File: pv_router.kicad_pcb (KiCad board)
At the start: 4 copper layers, 70 x 70 mm, 83 parts, among them IC1 AP63203WU-7, IC2 ATM90E26-YU-B, J1 Barrel_Jack_Switch_Pin3Ring, J10 Conn_01x03_Pin, J2 AudioJack3, J3 AudioJack3, J4 Barrel_Jack_Switch_Pin3Ring, J5 UART, J6 ToSSR, J7 USB_A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

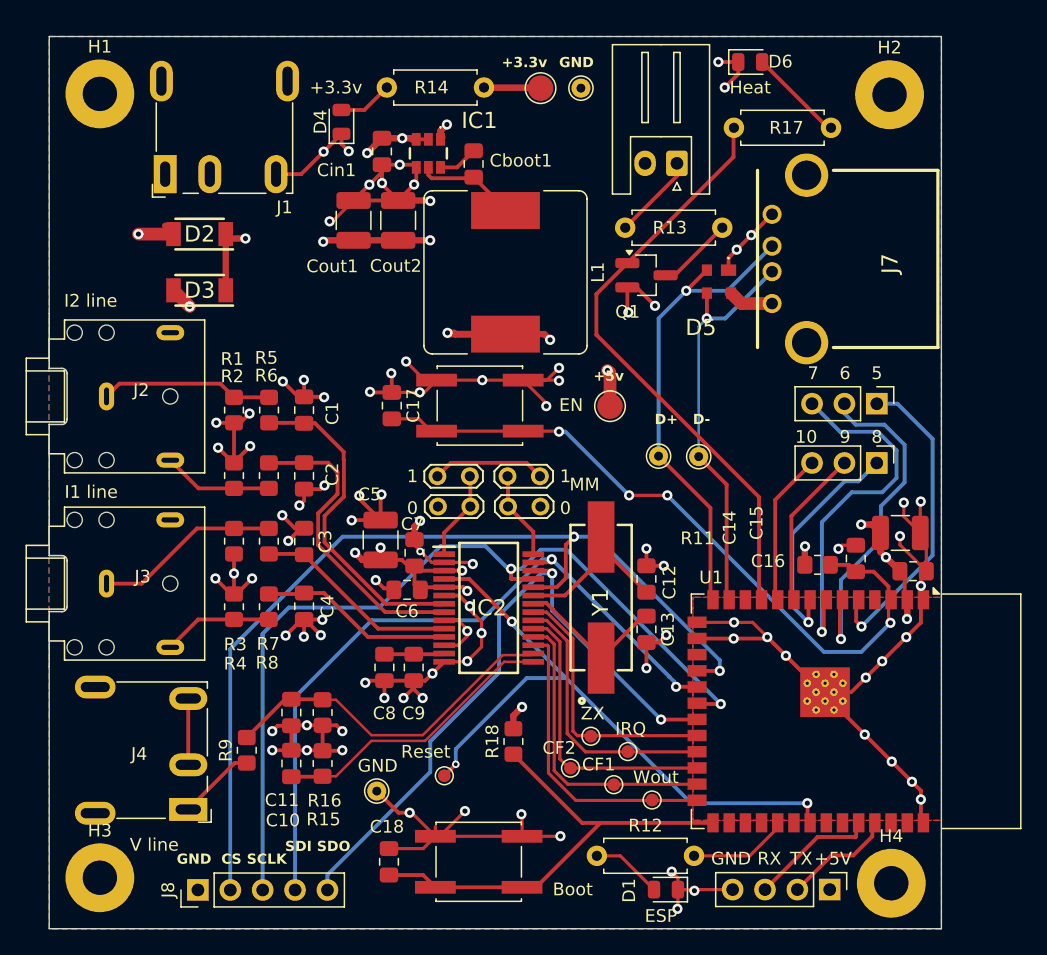
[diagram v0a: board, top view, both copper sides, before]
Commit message: fix: set SMT LED to 1206 size
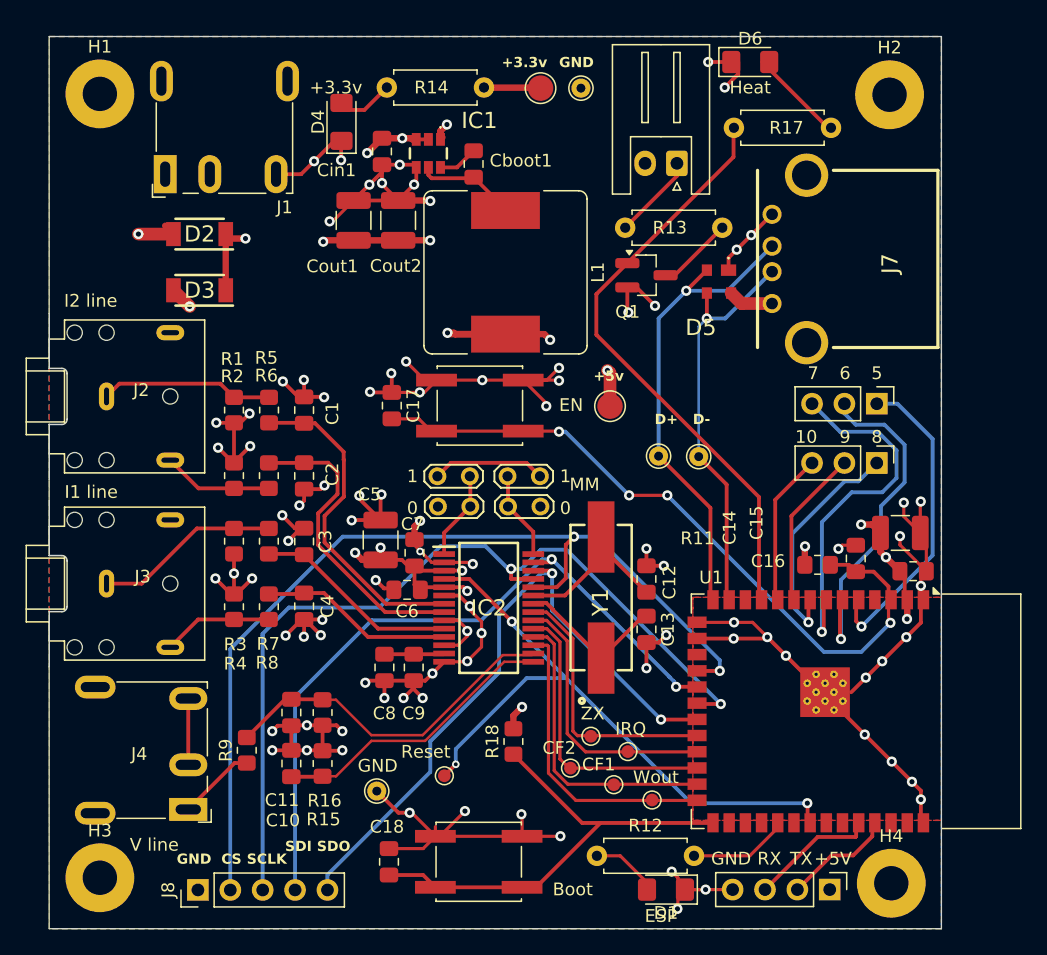
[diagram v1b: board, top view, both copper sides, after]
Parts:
- D1, D4, D6: footprint LED_SMD:LED_0805_2012Metric -> LED_SMD:LED_1206_3216Metric_Pad1.42x1.75mm_HandSolder
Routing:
- net GND: track 266.6 -> 268.7 mm

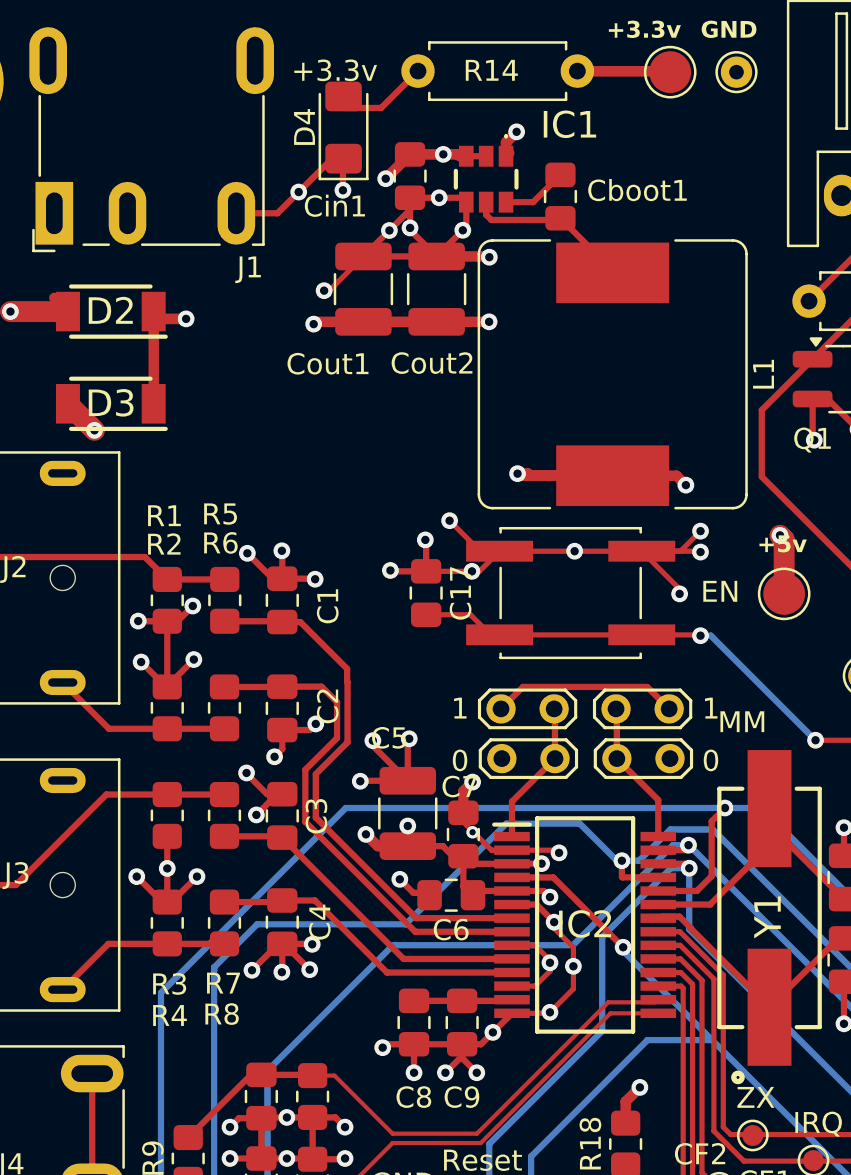
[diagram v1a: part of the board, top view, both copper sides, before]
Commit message: fix: zones under buck converter
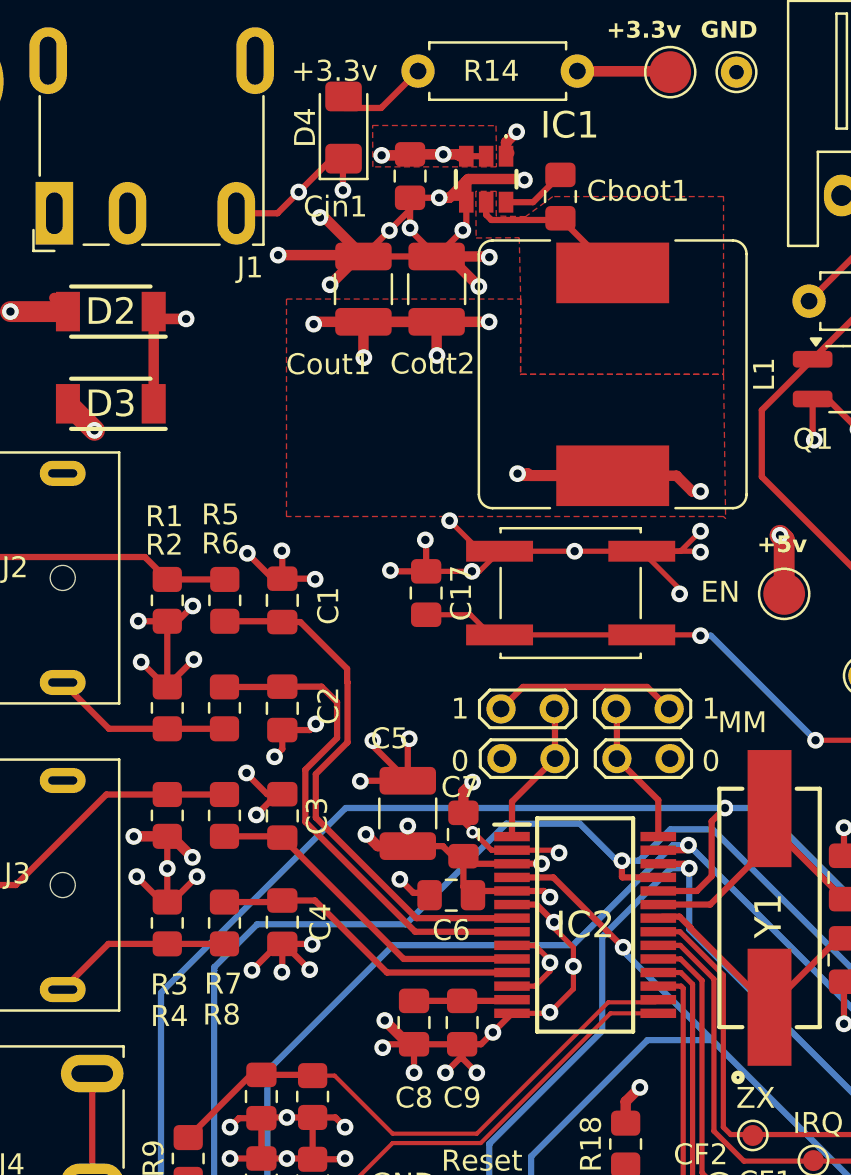
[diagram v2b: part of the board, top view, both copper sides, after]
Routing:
- net GND: track 268.7 -> 288.8 mm, vias 89 -> 96
- net +3V3: track 86.2 -> 90.4 mm, vias 14 -> 16
- net Net-(D2-K): track 23.8 -> 24.5 mm
- added copper zone on F.Cu, net +3V3
- added copper zone on F.Cu, net Net-(D2-K)
- added copper zone on F.Cu, net Net-(IC1-SW)

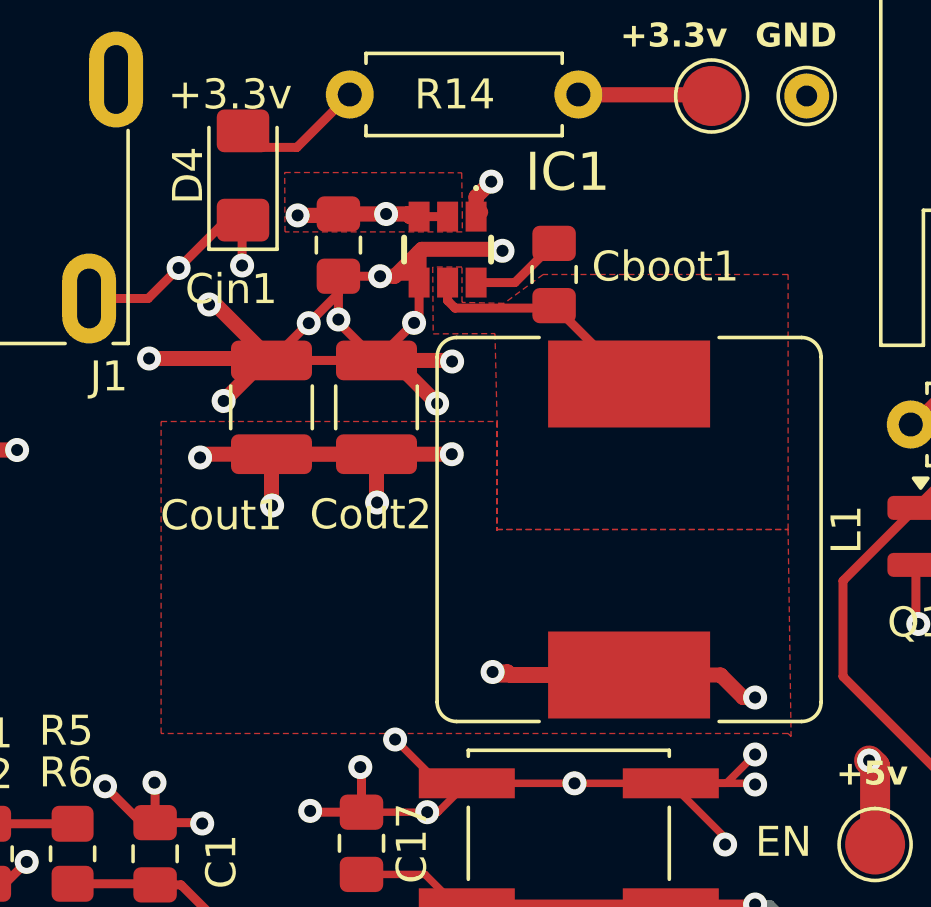
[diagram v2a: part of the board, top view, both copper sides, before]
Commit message: fix: add +3.3V vias btw F layer and layer 3
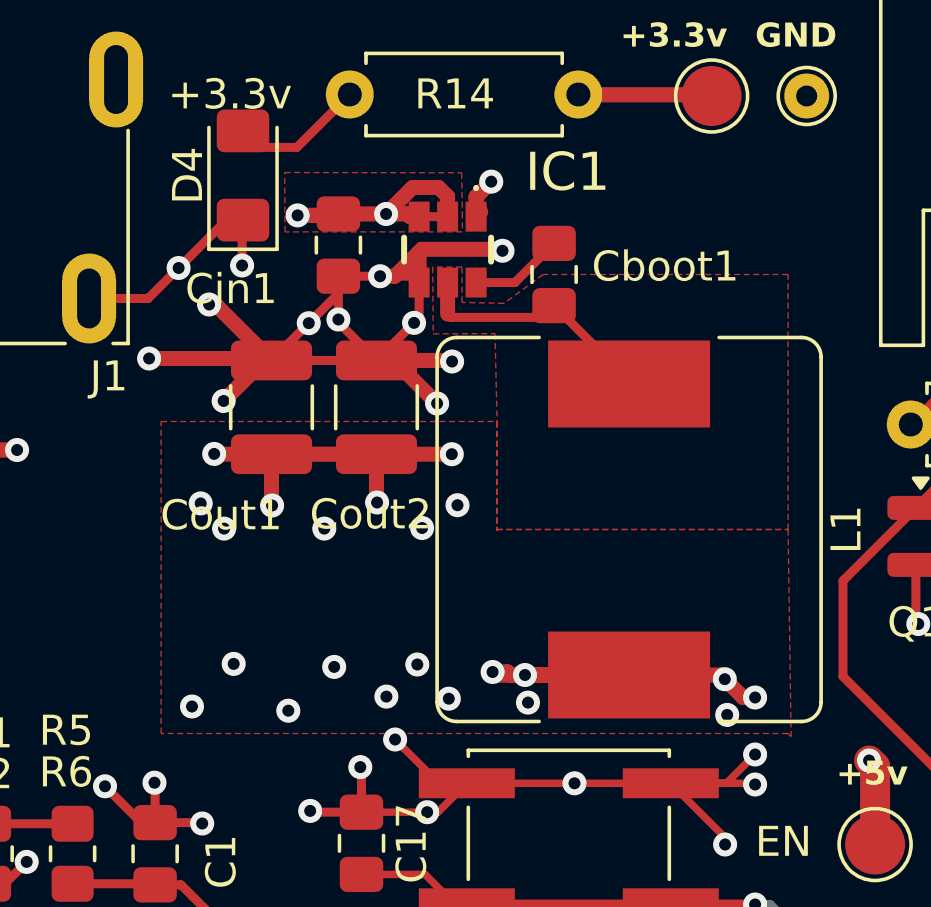
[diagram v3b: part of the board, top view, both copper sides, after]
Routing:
- net Net-(D2-K): track 24.5 -> 28.1 mm
- net Net-(IC1-SW): track 7.71 -> 8.34 mm
- net +3V3: track 90.4 -> 89.9 mm, vias 16 -> 32

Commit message: fix: reroute +12V track to enable direct +3.3V connections on buck converter pins
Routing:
- net +12V: track 55.5 -> 54.0 mm
- net +3V3: vias 32 -> 39

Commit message: fix: after DRC check
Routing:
- net +3V3: track 89.9 -> 90.6 mm
- net /adc/RESET: track 51.0 -> 51.5 mm
